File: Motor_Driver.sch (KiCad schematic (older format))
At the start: 16 parts, among them J3 M1, J4 M2, J5 PWR_IN, U1 TB67H420FTG_EL

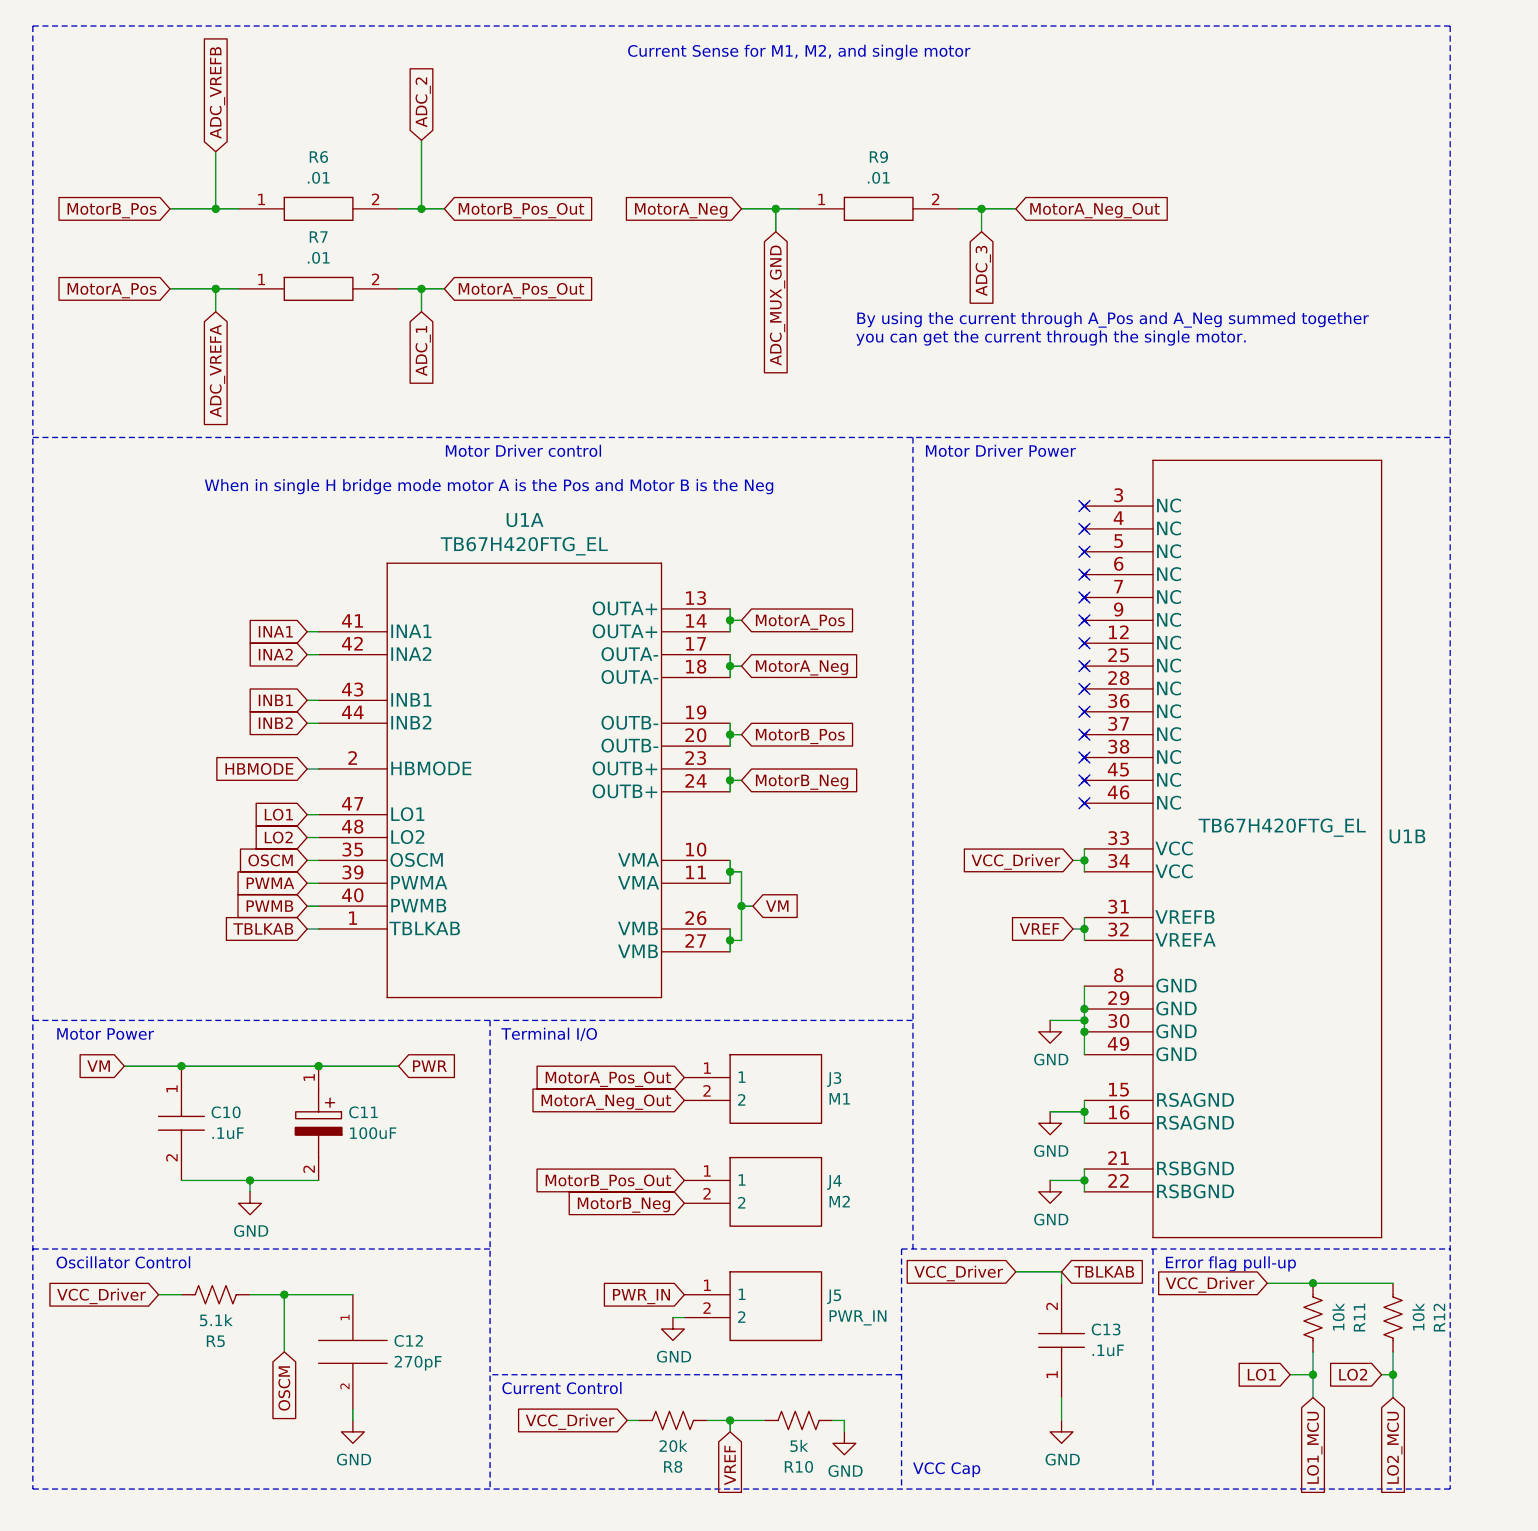
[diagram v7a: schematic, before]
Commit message: removed two current sense resistors and multiple unsused ADC pins
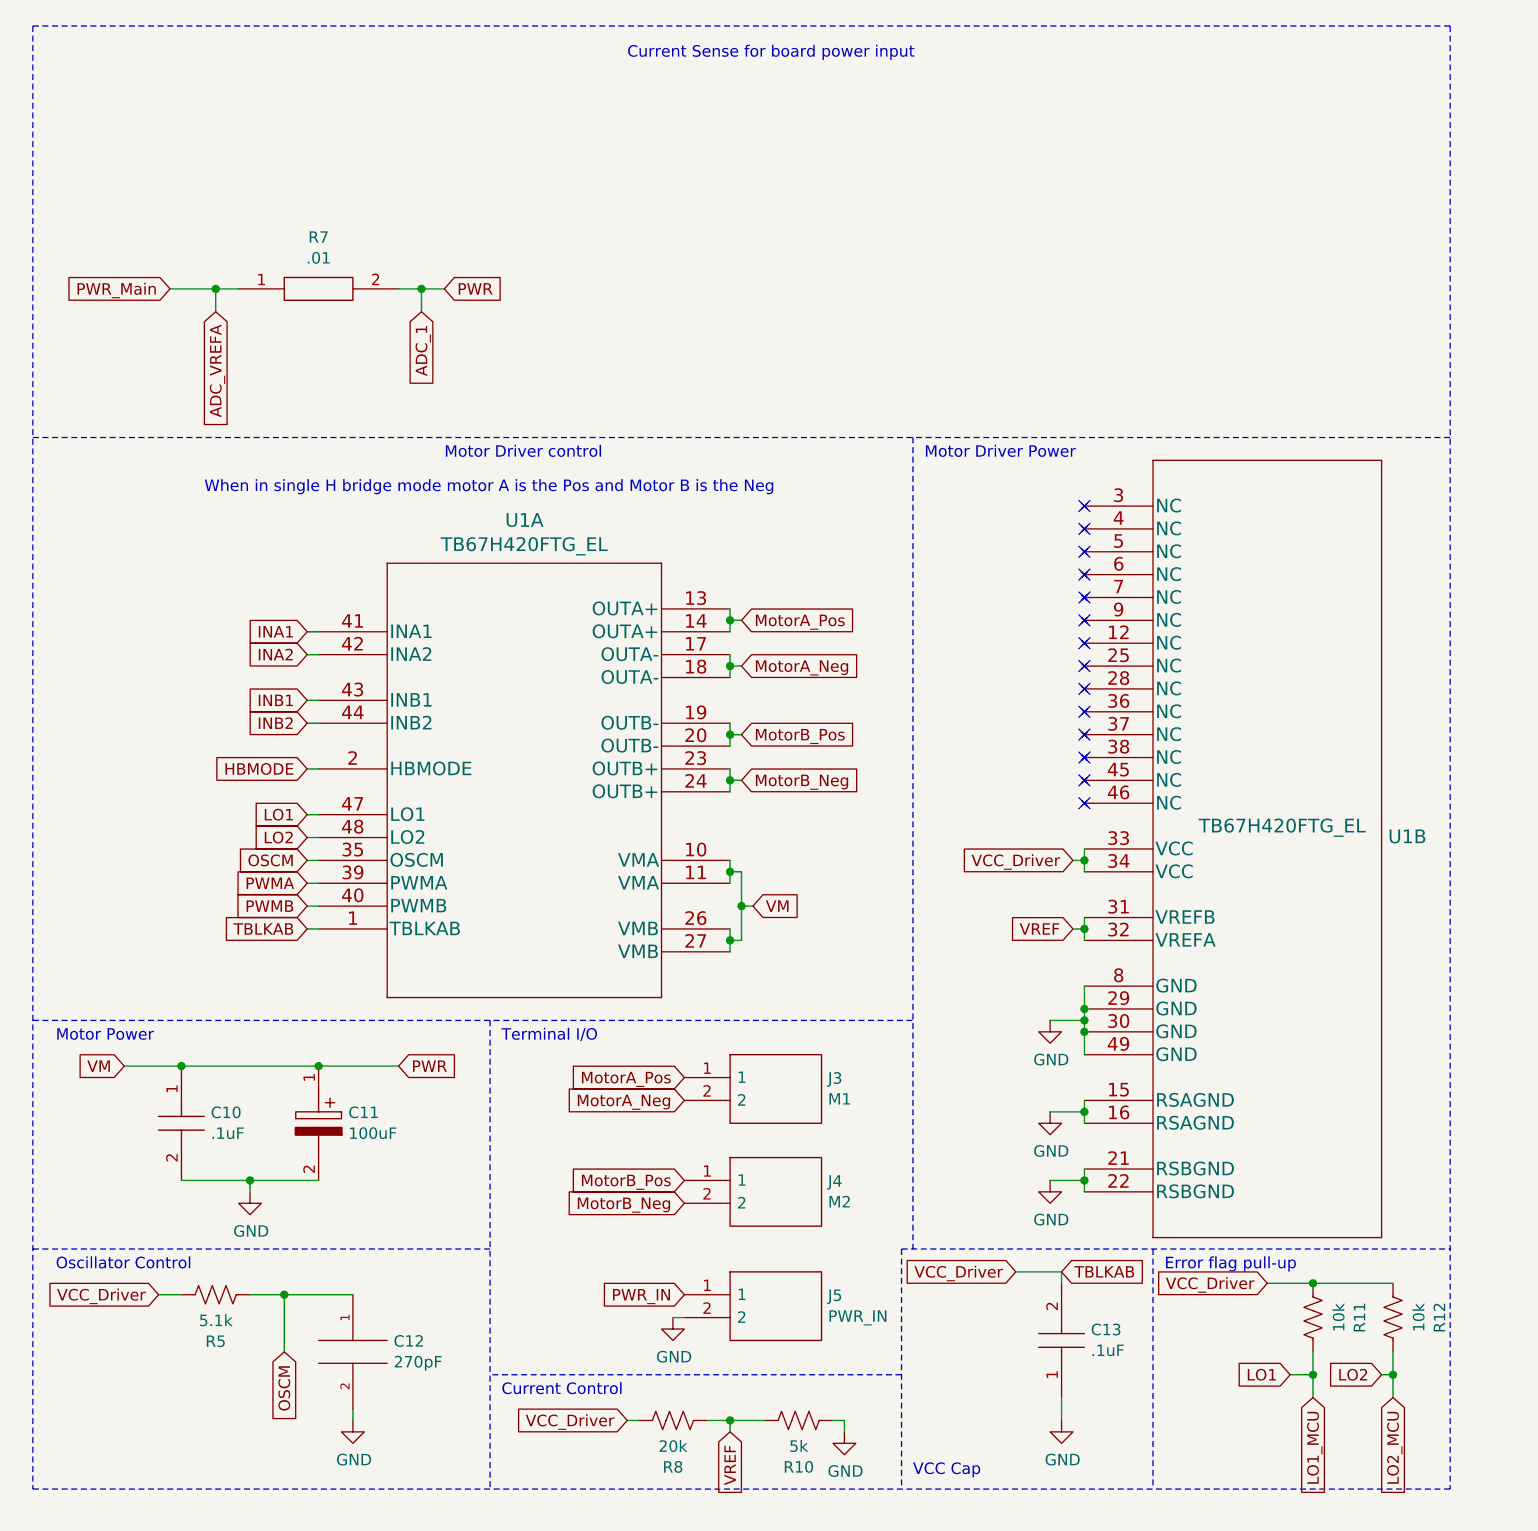
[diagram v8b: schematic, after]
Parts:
- removed R6, R9: .01, SamacSys_Parts:RESC6430X66N, symbol ESC_5A-rescue:PCS2512DR0100ET-SamacSys_Parts
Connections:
- net ADC_MUX_GND is gone; now on net MotorA_Neg: U1.17 (OUTA-), U1.18 (OUTA-)
- net ADC_VREFB is gone; now on net MotorB_Pos: U1.19 (OUTB-), U1.20 (OUTB-)
- net PWR is gone; now on net ADC_1: C10.1, C11.1, U1.10 (VMA), U1.11 (VMA), U1.26 (VMB), U1.27 (VMB)
- net ADC_1: no longer J3.1
- net ADC_VREFA: no longer U1.13 (OUTA+), U1.14 (OUTA+)
- net ADC_2 renamed MotorB_Pos
- net ADC_3 renamed MotorA_Neg
- new net MotorA_Pos: J3.1, U1.13 (OUTA+), U1.14 (OUTA+)
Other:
- note added: "Current Sense for board power input"
- note removed: "By using the current through A_Pos and A_Neg summed together\nyou can get the current through the single motor."
- note removed: "Current Sense for M1, M2, and single motor"
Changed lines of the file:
@@
 Text Notes 800  5750 0    50   ~ 0
 Motor Power
-Text GLabel 3550 5900 0    50   Input ~ 0
-MotorA_Pos_Out
-Text GLabel 3550 6000 0    50   Input ~ 0
-MotorA_Neg_Out
-Text GLabel 3550 6350 0    50   Input ~ 0
-MotorB_Pos_Out
 Text GLabel 3550 6450 0    50   Input ~ 0
 MotorB_Neg
@@
 	1    0    0    -1
 $EndComp
-Text GLabel 1300 2450 0    50   Input ~ 0
-MotorA_Pos
 Wire Wire Line
 	1300 2450 1500 2450
@@
 Text GLabel 1500 2550 3    50   Input ~ 0
 ADC_VREFA
-Text GLabel 1500 1850 1    50   Input ~ 0
-ADC_VREFB
 Text GLabel 2400 2550 3    50   Input ~ 0
 ADC_1
-Text GLabel 2400 1800 1    50   Input ~ 0
-ADC_2
-Wire Wire Line
-	2400 2100 2500 2100
-Connection ~ 2400 2100
-Wire Wire Line
-	2400 2100 2400 1800
-Wire Wire Line
-	1500 2100 1600 2100
-Connection ~ 1500 2100
-Wire Wire Line
-	1500 2100 1500 1850
-Wire Wire Line
-	2300 2100 2400 2100
-Wire Wire Line
-	1300 2100 1500 2100
-Text GLabel 1300 2100 0    50   Input ~ 0
-MotorB_Pos
-$Comp
-L ESC_5A-rescue:PCS2512DR0100ET-SamacSys_Parts R6
-U 1 1 60D7DF37
-P 1600 2100
-F 0 "R6" H 1950 2325 50  0000 C CNN
-F 1 ".01" H 1950 2234 50  0000 C CNN
-F 2 "SamacSys_Parts:RESC6430X66N" H 2150 2150 50  0001 L CNN
-F 3 "https://rs.componentsearchengine.com/Datasheets/2/PCS2512DR0100ET.pdf" H 2150 2050 50  0001 L CNN
-F 4 "Current Sense Resistors - SMD" H 2150 1950 50  0001 L CNN "Description"
-F 5 "0.664" H 2150 1850 50  0001 L CNN "Height"
-F 6 "588-PCS2512DR0100ET" H 2150 1750 50  0001 L CNN "Mouser Part Number"
-F 7 "https://www.mouser.co.uk/ProductDetail/Ohmite/PCS2512DR0100ET?qs=Zz7%252BYVVL6bF4W%2Fc9YcyG%2Fg%3D%3D" H 2150 1650 50  0001 L CNN "Mouser Price/Stock"
-F 8 "Ohmite" H 2150 1550 50  0001 L CNN "Manufacturer_Name"
-F 9 "PCS2512DR0100ET" H 2150 1450 50  0001 L CNN "Manufacturer_Part_Number"
-	1    1600 2100
-	1    0    0    -1
-$EndComp
-Text GLabel 2500 2100 2    50   Input ~ 0
-MotorB_Pos_Out
-Text GLabel 2500 2450 2    50   Input ~ 0
-MotorA_Pos_Out
 Wire Notes Line
 	700  5650 4550 5650
@@
 	700  1300 700  7700
 Text Notes 3300 1450 0    50   ~ 0
-Current Sense for M1, M2, and single motor
-$Comp
-L ESC_5A-rescue:PCS2512DR0100ET-SamacSys_Parts R9
-U 1 1 60DD4ABF
-P 4050 2100
-F 0 "R9" H 4400 2325 50  0000 C CNN
-F 1 ".01" H 4400 2234 50  0000 C CNN
-F 2 "SamacSys_Parts:RESC6430X66N" H 4600 2150 50  0001 L CNN
-F 3 "https://rs.componentsearchengine.com/Datasheets/2/PCS2512DR0100ET.pdf" H 4600 2050 50  0001 L CNN
-F 4 "Current Sense Resistors - SMD" H 4600 1950 50  0001 L CNN "Description"
-F 5 "0.664" H 4600 1850 50  0001 L CNN "Height"
-F 6 "588-PCS2512DR0100ET" H 4600 1750 50  0001 L CNN "Mouser Part Number"
-F 7 "https://www.mouser.co.uk/ProductDetail/Ohmite/PCS2512DR0100ET?qs=Zz7%252BYVVL6bF4W%2Fc9YcyG%2Fg%3D%3D" H 4600 1650 50  0001 L CNN "Mouser Price/Stock"
-F 8 "Ohmite" H 4600 1550 50  0001 L CNN "Manufacturer_Name"
-F 9 "PCS2512DR0100ET" H 4600 1450 50  0001 L CNN "Manufacturer_Part_Number"
-	1    4050 2100
-	1    0    0    -1
-$EndComp
-Text GLabel 3800 2100 0    50   Input ~ 0
-MotorA_Neg
-Text GLabel 5000 2100 2    50   Input ~ 0
-MotorA_Neg_Out
-Wire Wire Line
-	3800 2100 3950 2100
-Wire Wire Line
-	4750 2100 4850 2100
-Wire Wire Line
-	3950 2100 3950 2200
-Connection ~ 3950 2100
-Wire Wire Line
-	3950 2100 4050 2100
-Wire Wire Line
-	4850 2100 4850 2200
-Connection ~ 4850 2100
-Wire Wire Line
-	4850 2100 5000 2100
-Text GLabel 3950 2200 3    50   Input ~ 0
-ADC_MUX_GND
-Text GLabel 4850 2200 3    50   Input ~ 0
-ADC_3
+Current Sense for board power input
 Wire Notes Line
 	4550 3100 4550 6650
@@
 Wire Notes Line
 	700  1300 6900 1300
-Text Notes 4300 2700 0    50   ~ 0
-By using the current through A_Pos and A_Neg summed together\nyou can get the current through the single motor.
 $Comp
 L ESC_5A-rescue:C0805C104MMREC7210-SamacSys_Parts C10
@@
 Text GLabel 2300 5850 2    50   Input ~ 0
 PWR
+Text GLabel 1300 2450 0    50   Input ~ 0
+PWR_Main
+Text GLabel 2500 2450 2    50   Input ~ 0
+PWR
+Text GLabel 3550 5900 0    50   Input ~ 0
+MotorA_Pos
+Text GLabel 3550 6000 0    50   Input ~ 0
+MotorA_Neg
+Text GLabel 3550 6350 0    50   Input ~ 0
+MotorB_Pos
 $EndSCHEMATC
